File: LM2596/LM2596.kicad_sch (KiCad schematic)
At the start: 5 parts, among them U1 LM2596S-5

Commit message: Footprint e PCB
Assegnazione delle footprint a tutti i componenti e collocato il tutto nel file PCB
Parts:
- C1, C2: footprint (none) -> Capacitor_SMD:CP_Elec_3x5.3
- D1: footprint (none) -> Diode_SMD:D_0201_0603Metric
- L1: footprint (none) -> Inductor_SMD:L_6.3x6.3_H3
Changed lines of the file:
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@@
       (effects (font (size 1.27 1.27)) (justify left))
     )
-    (property "Footprint" "" (id 2) (at 134.62 46.99 0)
+    (property "Footprint" "Diode_SMD:D_0201_0603Metric" (id 2) (at 134.62 46.99 0)
       (effects (font (size 1.27 1.27)) hide)
     )
@@
       (effects (font (size 1.27 1.27)) (justify left))
     )
-    (property "Footprint" "" (id 2) (at 92.4052 38.1 0)
+    (property "Footprint" "Capacitor_SMD:CP_Elec_3x5.3" (id 2) (at 92.4052 38.1 0)
       (effects (font (size 1.27 1.27)) hide)
     )
@@
       (effects (font (size 1.27 1.27)) (justify left))
     )
-    (property "Footprint" "" (id 2) (at 174.9552 52.07 0)
+    (property "Footprint" "Capacitor_SMD:CP_Elec_3x5.3" (id 2) (at 174.9552 52.07 0)
       (effects (font (size 1.27 1.27)) hide)
     )
@@
     (property "Reference" "L1" (id 0) (at 153.67 48.26 0))
     (property "Value" "33uH" (id 1) (at 153.67 45.72 0))
-    (property "Footprint" "" (id 2) (at 153.67 43.18 0)
+    (property "Footprint" "Inductor_SMD:L_6.3x6.3_H3" (id 2) (at 153.67 43.18 0)
       (effects (font (size 1.27 1.27)) hide)
     )
@@
     )
     (path "/31b33049-67c8-4a90-b779-26e69b464680"
-      (reference "C1") (unit 1) (value "680uF") (footprint "")
+      (reference "C1") (unit 1) (value "680uF") (footprint "Capacitor_SMD:CP_Elec_3x5.3")
     )
     (path "/daf88303-093a-45a2-9860-ebe493f72555"
-      (reference "C2") (unit 1) (value "220uF") (footprint "")
+      (reference "C2") (unit 1) (value "220uF") (footprint "Capacitor_SMD:CP_Elec_3x5.3")
     )
     (path "/06d5bc34-7358-498b-a275-01a429b9644f"
-      (reference "D1") (unit 1) (value "D_Zener") (footprint "")
+      (reference "D1") (unit 1) (value "D_Zener") (footprint "Diode_SMD:D_0201_0603Metric")
     )
     (path "/e843d02e-1d5b-4d23-8f38-162dda1614d4"
-      (reference "L1") (unit 1) (value "33uH") (footprint "")
+      (reference "L1") (unit 1) (value "33uH") (footprint "Inductor_SMD:L_6.3x6.3_H3")
     )
     (path "/662d98f6-225d-4847-a857-be3d647a865a"

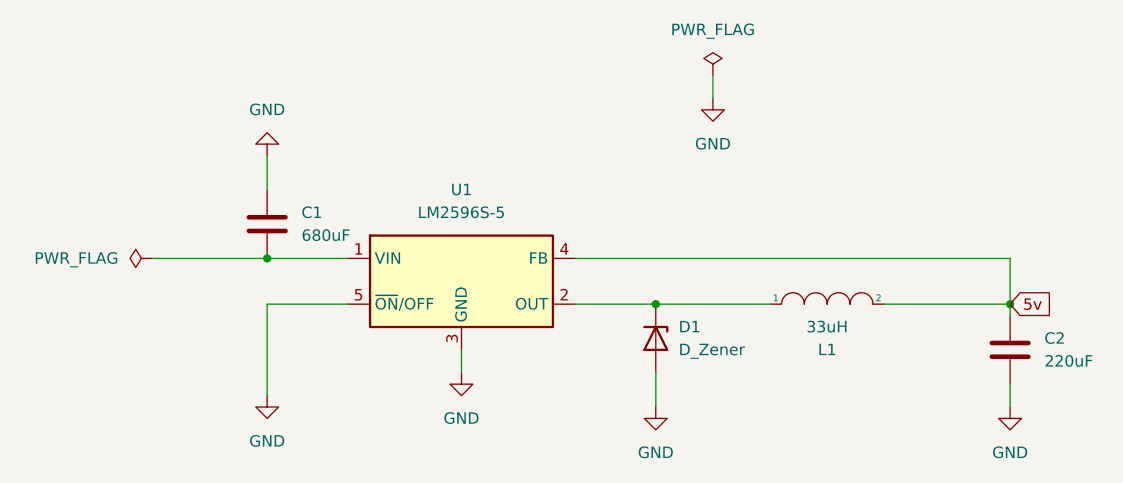
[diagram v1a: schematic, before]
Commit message: 13/10/2022
Sistemato lo schema elettrico.
Creato le tracce nel file PCB.
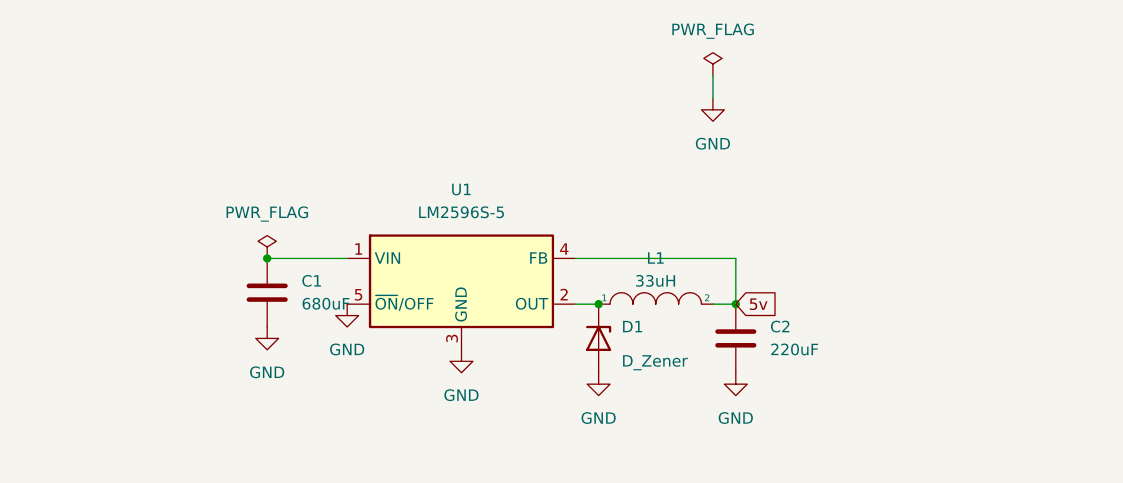
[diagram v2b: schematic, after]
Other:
- moved on the sheet: C1, C2, D1, L1
